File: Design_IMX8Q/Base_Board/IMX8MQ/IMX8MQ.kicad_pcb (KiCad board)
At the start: 8 copper layers, 50.2 x 82 mm, 102 parts, among them Q1 AO3401A, U1 MIMX8MQ6CVAHZAB, U10 PCMF3USB3S, U11 PCMF3USB3S, U12 PCMF3USB3S, U13 KSZ9131RNXI, U14 IMX6ModuleConector_300, U2 IS43LQ32256A-062BLI, U4 MP8759GD-Z, U5 MP2263GD-Z, U6 SDINBDG4-8G, U7 MT25QUxxxxxx1xW7, U9 PTN36043ABXY, X1 ABLNO, Y1 27MHz, Y2 25MHz

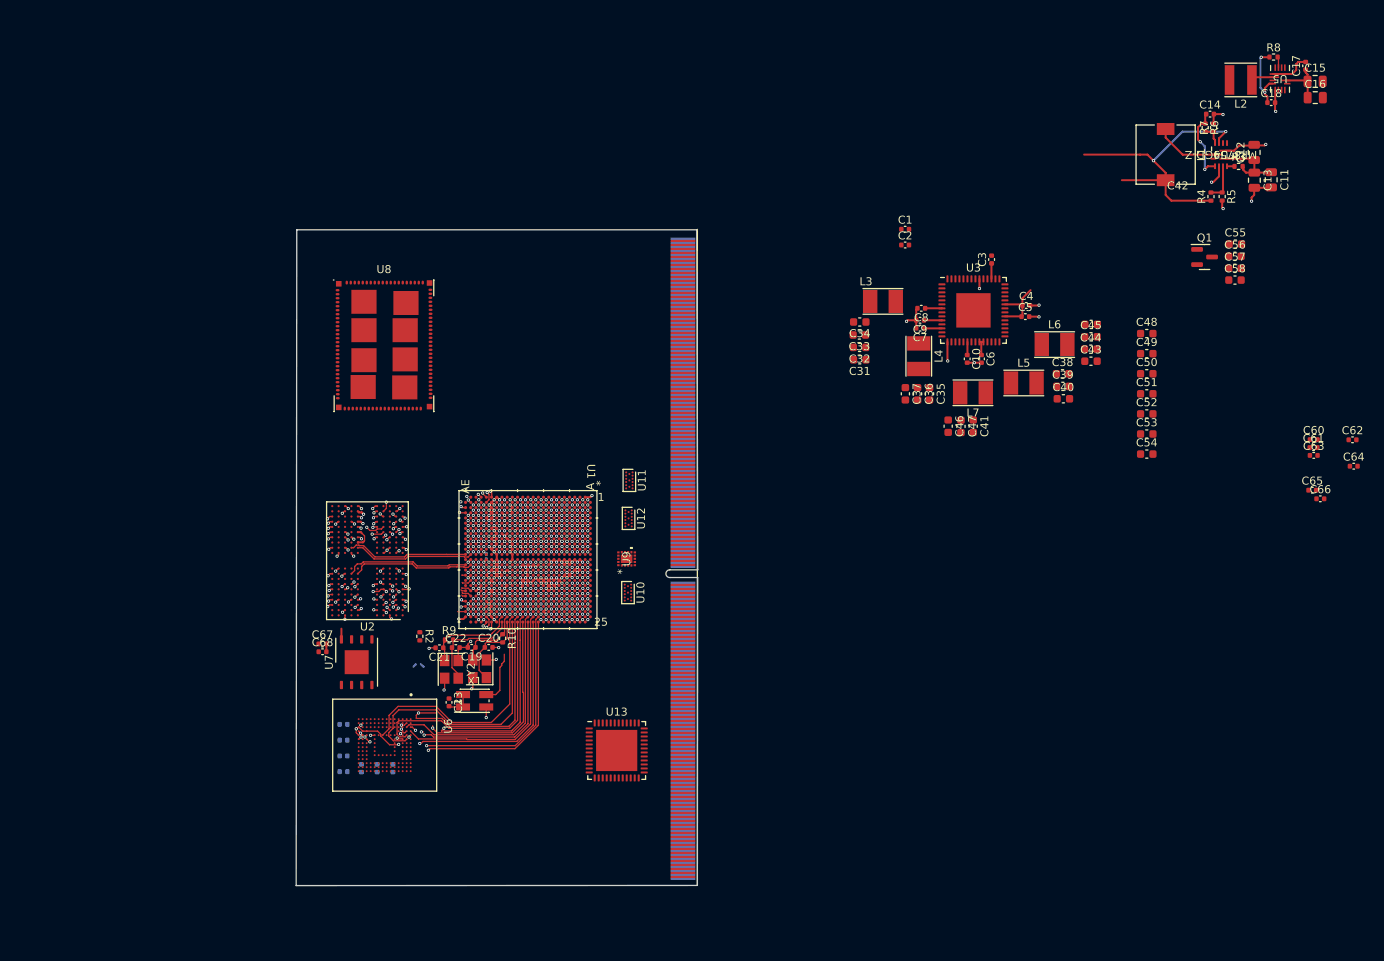
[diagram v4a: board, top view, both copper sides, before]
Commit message: Add QSPI and more color
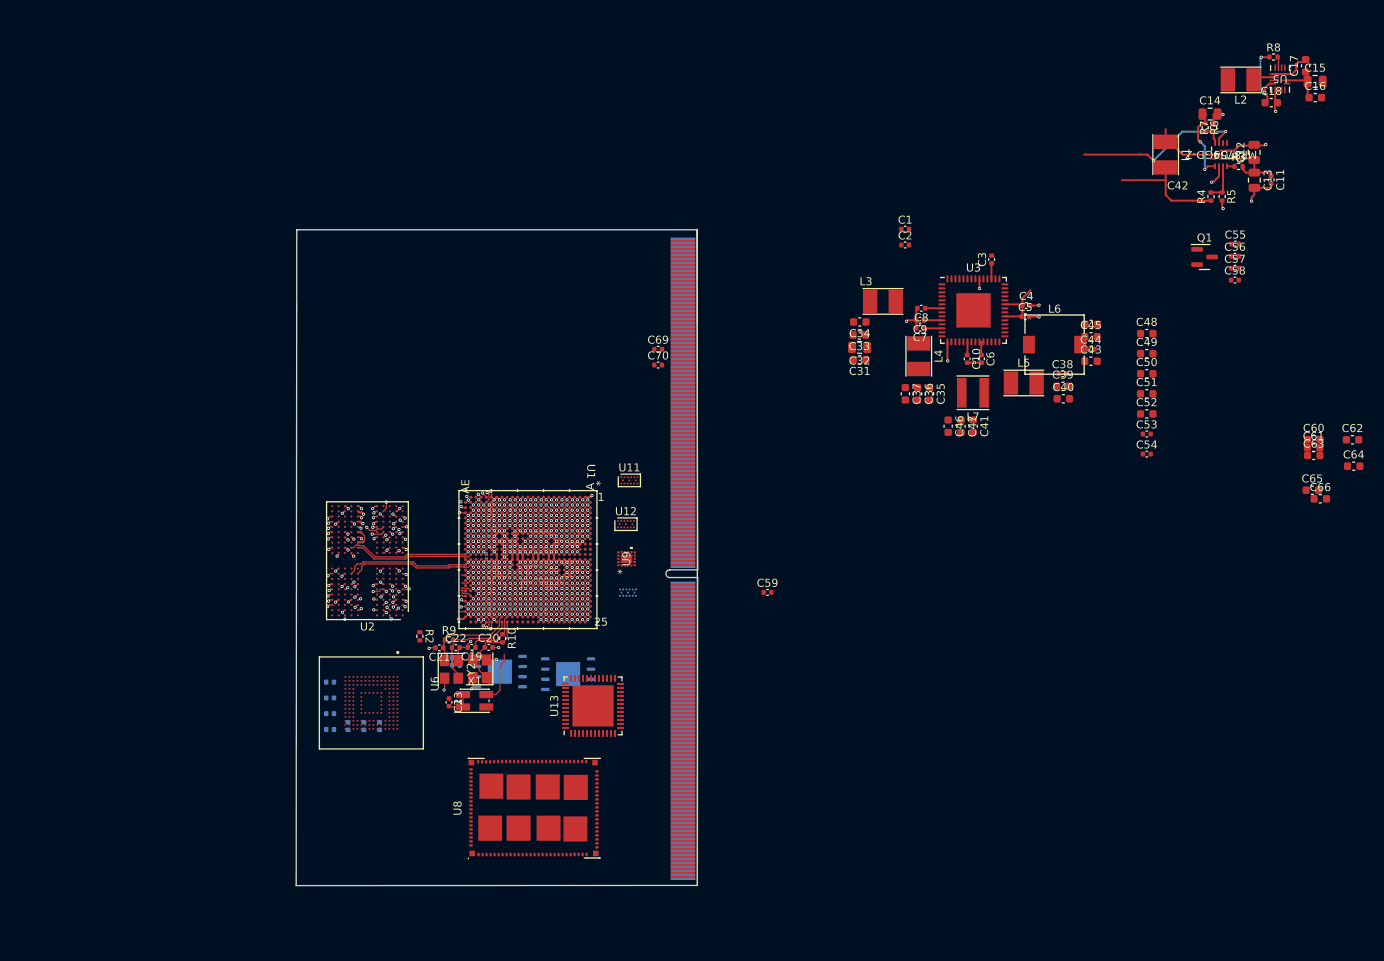
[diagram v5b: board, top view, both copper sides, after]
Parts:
- added C59: 0.1uF, Capacitor_SMD:C_0402_1005Metric, F.Cu at (116.7, 87.0)
- added C69: 0.1uF, Capacitor_SMD:C_0402_1005Metric, F.Cu at (103.0, 56.6)
- added C70: 0.1uF, Capacitor_SMD:C_0402_1005Metric, F.Cu at (103.0, 58.6)
- added U15: MT25QUxxxxxx1xW7, Package_DFN_QFN:W-PDFN-8-1EP_6x5mm_P1.27mm_EP3x3mm, B.Cu at (91.8, 97.2)
- C11: footprint Capacitor_SMD:C_0805_2012Metric -> Capacitor_SMD:C_0402_1005Metric
- C14: footprint Capacitor_SMD:C_0402_1005Metric -> Capacitor_SMD:C_0805_2012Metric
- C16: value 10uF -> 22uF; footprint Capacitor_SMD:C_0805_2012Metric -> Capacitor_SMD:C_0603_1608Metric
- C17: value 0.1uF -> 22uF; footprint Capacitor_SMD:C_0402_1005Metric -> Capacitor_SMD:C_0603_1608Metric
- C18: value 1uF -> 22uF; footprint Capacitor_SMD:C_0402_1005Metric -> Capacitor_SMD:C_0603_1608Metric
- C32: value 22uF -> 10uF; footprint Capacitor_SMD:C_0603_1608Metric -> Capacitor_SMD:C_0805_2012Metric
- C38, C58: value 22uF -> 0.1uF; footprint Capacitor_SMD:C_0603_1608Metric -> Capacitor_SMD:C_0402_1005Metric
- C44: value 22uF -> 1uF; footprint Capacitor_SMD:C_0603_1608Metric -> Capacitor_SMD:C_0402_1005Metric
- C49, C50, C51, C52: value 4.7uF -> 22uF
- C53: value 4.7uF -> 1uF; footprint Capacitor_SMD:C_0603_1608Metric -> Capacitor_SMD:C_0402_1005Metric
- C54: value 1uF -> 0.1uF; footprint Capacitor_SMD:C_0603_1608Metric -> Capacitor_SMD:C_0402_1005Metric
- C55, C56, C57: value 22uF -> 0.47uF; footprint Capacitor_SMD:C_0603_1608Metric -> Capacitor_SMD:C_0402_1005Metric
- C60, C61, C62: value 0.47uF -> 4.7uF; footprint Capacitor_SMD:C_0402_1005Metric -> Capacitor_SMD:C_0603_1608Metric
- C63: value 1uF -> 4.7uF; footprint Capacitor_SMD:C_0402_1005Metric -> Capacitor_SMD:C_0603_1608Metric
- C64, C65: value 0.1uF -> 4.7uF; footprint Capacitor_SMD:C_0402_1005Metric -> Capacitor_SMD:C_0603_1608Metric
- C66: value 0.1uF -> 1uF; footprint Capacitor_SMD:C_0402_1005Metric -> Capacitor_SMD:C_0603_1608Metric
- C67, C68, U10, U7: moved to B.Cu
- L1: value 1.5uH -> 1uH; footprint Inductor_SMD:L_7.3x7.3_H4.5 -> Inductor_SMD:L_Taiyo-Yuden_NR-30xx_HandSoldering
- L2: value 4.7uH -> 1uH; footprint Inductor_SMD:L_Taiyo-Yuden_NR-40xx -> Inductor_SMD:L_Taiyo-Yuden_NR-30xx_HandSoldering
- L6: value 1uH -> 1.5uH; footprint Inductor_SMD:L_Taiyo-Yuden_NR-30xx_HandSoldering -> Inductor_SMD:L_7.3x7.3_H4.5
- L7: value 1uH -> 4.7uH; footprint Inductor_SMD:L_Taiyo-Yuden_NR-30xx_HandSoldering -> Inductor_SMD:L_Taiyo-Yuden_NR-40xx
- R3: value 1.5M -> 100k
- R4: value 44.2K -> 100k
- R5: value 9.53k -> 1.5M
- R6: value 100k -> 44.2K
- R7: value 100k -> 9.53k
- moved U8 60.8 mm to (87.5, 114.0), turned to 90 degrees
- moved U7 17.9 mm to (83.2, 96.9), turned to 0 degrees
- moved C67 16.8 mm to (77.7, 95.1), turned to 180 degrees
- moved C68 16.8 mm to (77.7, 96.1), turned to 180 degrees
- moved U13 6.31 mm to (94.9, 101.2), turned to 90 degrees
- moved C24 5.54 mm to (62.0, 104.1)
- moved C25 5.54 mm to (62.0, 102.2)
- moved C26 5.54 mm to (62.0, 100.2)
- moved C27 5.54 mm to (62.0, 98.2)
- moved C28 5.54 mm to (64.2, 103.7)
- moved C29 5.54 mm to (66.2, 103.7)
- moved C30 5.54 mm to (68.2, 103.7)
- moved U6 5.54 mm to (67.2, 100.8)
- moved U12 0.79 mm to (99.0, 78.5), turned to 0 degrees
- turned U10 to 0 degrees
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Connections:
- C11 pad 1: VSYS -> Net-(U4-VCC)
- C14 pad 1: Net-(U4-VCC) -> VSYS
- C16 pad 1: VSYS -> VDD_GPU_0V9
- C17 pad 1: VSYS -> VDD_VPU_0V9
- C18 pad 1: Net-(U5-VCC) -> NVCC_DRAM_1V1
- C28 pad 2: VDD_3V3 -> NVCC_3V3
- C29 pad 2: VDD_3V3 -> NVCC_3V3
- C30 pad 2: VDD_3V3 -> NVCC_3V3
- C31 pad 1: VDD_GPU_0V9 -> NVCC_SD1_1V8
- C32 pad 1: VDD_GPU_0V9 -> VSYS
- C33 pad 1: VDD_GPU_0V9 -> Net-(U3A-SW3AFB)
- C36 pad 1: VDD_VPU_0V9 -> NVCC_DRAM_1V1
- C37 pad 1: VDD_VPU_0V9 -> NVCC_SD1_1V8
- C38 pad 1: NVCC_DRAM_1V1 -> VSYS
- C39 pad 1: NVCC_DRAM_1V1 -> Net-(U3A-SW3AFB)
- C40 pad 1: NVCC_DRAM_1V1 -> VDD_GPU_0V9
- C41 pad 1: NVCC_SD1_1V8 -> VDD_VPU_0V9
- C42 pad 1: Net-(U3A-SW3AFB) -> NVCC_DRAM_1V1
- C43 pad 1: Net-(U3A-SW3AFB) -> NVCC_SD1_1V8
- C44 pad 1: Net-(U3A-SW3AFB) -> Net-(U5-VCC)
- C46 pad 1: NVCC_SD1_1V8 -> VDD_GPU_0V9
- C47 pad 1: NVCC_SD1_1V8 -> Net-(U3A-SW3AFB)
- C49 pad 1: Net-(U3C-VGEN2) -> DCDC_3V3
- C50 pad 1: Net-(U3C-VGEN3) -> DCDC_3V3
- C51 pad 1: Net-(U3C-VGEN4) -> DCDC_3V3
- C52 pad 1: Net-(U3C-VGEN6) -> DCDC_3V3
- C53 pad 1: Net-(U3C-VSNVS) -> DCDC_3V3
- C54 pad 1: Net-(U3C-VREFDDR) -> Net-(U3C-LICELL)
- C57 pad 1: DCDC_3V3 -> Net-(U3C-VIN3)
- C58 pad 1: DCDC_3V3 -> NVCC_DRAM_1V1
- C58 pad 2: GND -> Net-(U3C-VHALF)
- C60 pad 1: DCDC_3V3 -> Net-(U3C-VGEN1)
- C61 pad 1: DCDC_3V3 -> Net-(U3C-VGEN2)
- C62 pad 1: Net-(U3C-VIN3) -> Net-(U3C-VGEN3)
- C63 pad 1: DCDC_3V3 -> Net-(U3C-VGEN4)
- C64 pad 1: Net-(U3C-LICELL) -> Net-(U3C-VGEN6)
- C65 pad 1: NVCC_DRAM_1V1 -> Net-(U3C-VSNVS)
- C65 pad 2: Net-(U3C-VHALF) -> GND
- C66 pad 1: Net-(U3C-VHALF) -> Net-(U3C-VREFDDR)
- C67 pad 2: VDD_3V3 -> NVCC_3V3
- C68 pad 2: VDD_3V3 -> NVCC_3V3
- L1 pad 1: Net-(U4-SW) -> Net-(U3A-SW1ALX)
- L1 pad 2: DCDC_3V3 -> VDD_GPU_0V9
- L2 pad 1: Net-(U5-SW) -> Net-(U3A-SW1CLX)
- L2 pad 2: DCDC_5V -> VDD_VPU_0V9
- L3 pad 1: Net-(U3A-SW1ALX) -> Net-(U3A-SW2LX)
- L3 pad 2: VDD_GPU_0V9 -> NVCC_DRAM_1V1
- L4 pad 1: Net-(U3A-SW1CLX) -> Net-(U3A-SW4LX)
- L4 pad 2: VDD_VPU_0V9 -> NVCC_SD1_1V8
- L5 pad 1: Net-(U3A-SW2LX) -> Net-(U3A-SW3ALX)
- L5 pad 2: NVCC_DRAM_1V1 -> Net-(U3A-SW3AFB)
- L6 pad 1: Net-(U3A-SW3ALX) -> Net-(U4-SW)
- L6 pad 2: Net-(U3A-SW3AFB) -> DCDC_3V3
- L7 pad 1: Net-(U3A-SW4LX) -> Net-(U5-SW)
- L7 pad 2: NVCC_SD1_1V8 -> DCDC_5V
- Q1 pad 2: VDD_3V3 -> NVCC_3V3
- R3 pad 1: Net-(U4-EN) -> Net-(U4-VCC)
- R3 pad 2: VSYS -> Net-(U4-MODE)
- R4 pad 1: DCDC_3V3 -> Net-(U4-MODE)
- R4 pad 2: Net-(U4-FB) -> GND
- R5 pad 1: Net-(U4-FB) -> Net-(U4-EN)
- R5 pad 2: GND -> VSYS
- R6 pad 1: Net-(U4-VCC) -> DCDC_3V3
- R6 pad 2: Net-(U4-MODE) -> Net-(U4-FB)
- R7 pad 1: Net-(U4-MODE) -> Net-(U4-FB)
- U1 pad A5: unconnected-(U1B-ECSPI2_SS0-PadA5) -> ECSPI2_SS0
- U1 pad A7: unconnected-(U1E-UART1_TXD-PadA7) -> UART1_TXD
- U1 pad AB3: Net-(U1G-NVCC_DRAM-PadAA10) -> NVCC_DRAM_1V1
- U1 pad AB8: Net-(U1G-NVCC_DRAM-PadAA10) -> NVCC_DRAM_1V1
- U1 pad AC3: Net-(U1G-NVCC_DRAM-PadAA10) -> NVCC_DRAM_1V1
- U1 pad AC6: Net-(U1G-NVCC_DRAM-PadAA10) -> NVCC_DRAM_1V1
- U1 pad AC8: Net-(U1G-NVCC_DRAM-PadAA10) -> NVCC_DRAM_1V1
- U1 pad AD5: Net-(U1G-NVCC_DRAM-PadAA10) -> NVCC_DRAM_1V1
- U1 pad B11: unconnected-(U1F-USB2_RESREF-PadB11) -> USB2_VBUS
- U1 pad B2: unconnected-(U1E-SAI1_TXD2-PadB2) -> SAI1_TXD2
- U1 pad B3: unconnected-(U1E-SAI1_TXD6-PadB3) -> SAI1_TXD6
- U1 pad B5: unconnected-(U1B-ECSPI2_MISO-PadB5) -> ECSPI2_MISO
- U1 pad B6: unconnected-(U1E-UART2_RXD-PadB6) -> UART2_RXD
- U1 pad C1: unconnected-(U1E-SAI1_TXD7-PadC1) -> SAI1_TXD7
- U1 pad C11: unconnected-(U1H-USB2_VPTX-PadC11) -> Net-(U1H-USB1_DVDD)
- U1 pad C12: unconnected-(U1H-USB1_VPTX-PadC12) -> Net-(U1H-USB1_DVDD)
- U1 pad C18: unconnected-(U1G-MIPI_VDDHA-PadC18) -> VDD_PHY_1V8
- U1 pad C2: unconnected-(U1E-SAI1_TXD5-PadC2) -> SAI1_TXD5
- U1 pad C3: unconnected-(U1E-SAI3_TXD-PadC3) -> SAI3_TXD
- U1 pad C4: unconnected-(U1E-SAI3_TXC-PadC4) -> SAI3_TXC
- U1 pad C5: unconnected-(U1B-ECSPI2_SCLK-PadC5) -> ECSPI2_SCLK
- U1 pad C6: unconnected-(U1E-UART4_RXD-PadC6) -> UART2_CTS_B
- U1 pad C7: unconnected-(U1E-UART1_RXD-PadC7) -> UART1_RXD
- U1 pad C9: unconnected-(U1F-USB2_ID-PadC9) -> USB2_ID
- U1 pad D1: unconnected-(U1E-SAI1_TXD3-PadD1) -> SAI1_TXD3
- U1 pad D11: unconnected-(U1H-USB2_VP-PadD11) -> Net-(U1H-USB1_DVDD)
- U1 pad D12: unconnected-(U1H-USB1_VP-PadD12) -> Net-(U1H-USB1_DVDD)
- U1 pad D17: unconnected-(U1G-MIPI_VDDHA-PadD17) -> VDD_PHY_1V8
- U1 pad D18: unconnected-(U1G-MIPI_VDDHA-PadD18) -> VDD_PHY_1V8
- U1 pad D2: unconnected-(U1E-SAI1_TXD4-PadD2) -> SAI1_TXD4
- U1 pad D3: unconnected-(U1E-SAI3_MCLK-PadD3) -> SAI3_MCLK
- U1 pad D6: unconnected-(U1E-UART2_TXD-PadD6) -> UART2_TXD
- U1 pad D7: unconnected-(U1E-UART4_TXD-PadD7) -> UART2_RTS_B
- U1 pad D8: unconnected-(U1H-NVCC_UART-PadD8) -> NVCC_3V3
- U1 pad D9: unconnected-(U1F-USB2_VBUS-PadD9) -> USB2_VBUS
- U1 pad E11: unconnected-(U1H-USB2_DVDD-PadE11) -> Net-(U1H-USB1_DVDD)
- U1 pad E12: unconnected-(U1H-USB1_DVDD-PadE12) -> Net-(U1H-USB1_DVDD)
- U1 pad E15: unconnected-(U1G-MIPI_VDD-PadE15) -> VDD_PHY_1V8
- U1 pad E17: unconnected-(U1G-MIPI_VDDA-PadE17) -> VDD_PHY_1V8
- U1 pad E18: unconnected-(U1G-MIPI_VDDA-PadE18) -> VDD_PHY_1V8
- U1 pad E2: unconnected-(U1E-SAI1_TXD1-PadE2) -> SAI1_TXD1
- U1 pad E3: unconnected-(U1H-NVCC_SAI3-PadE3) -> NVCC_3V3
- U1 pad E5: unconnected-(U1B-ECSPI2_MOSI-PadE5) -> ECSPI2_MOSI
- U1 pad E7: unconnected-(U1C-I2C1_SCL-PadE7) -> I2C1_SCL
- U1 pad E8: unconnected-(U1C-I2C1_SDA-PadE8) -> I2C1_SDA
- U1 pad E9: unconnected-(U1C-I2C3_SDA-PadE9) -> I2C3_SDA
- U1 pad F1: unconnected-(U1E-SAI1_RXD5-PadF1) -> SAI1_RXD5
- U1 pad F11: unconnected-(U1H-USB2_VPH-PadF11) -> NVCC_3V3
- U1 pad F12: unconnected-(U1H-USB1_VPH-PadF12) -> NVCC_3V3
- U1 pad F15: unconnected-(U1G-MIPI_VDD-PadF15) -> VDD_PHY_1V8
- U1 pad F17: unconnected-(U1G-MIPI_VDDA-PadF17) -> VDD_PHY_1V8
- U1 pad F18: unconnected-(U1G-MIPI_VDDA-PadF18) -> VDD_PHY_1V8
- U1 pad F19: unconnected-(U1G-MIPI_VDDPLL-PadF19) -> VDD_PHY_1V8
- U1 pad F2: unconnected-(U1E-SAI1_TXD0-PadF2) -> SAI1_TXD0
- U1 pad F21: unconnected-(U1D-NAND_CE2_B-PadF21) -> NAND_CE2_B
- U1 pad F22: unconnected-(U1H-PCIE_VP-PadF22) -> VDD_PHY_0V9
- U1 pad F23: unconnected-(U1H-PCIE_VPTXC-PadF23) -> VDD_PHY_0V9
- U1 pad F3: unconnected-(U1E-SAI3_RXD-PadF3) -> SAI3_RXD
- U1 pad F4: unconnected-(U1E-SAI3_RXC-PadF4) -> SAI3_RXC
- U1 pad F5: unconnected-(U1H-NVCC_ECSPI-PadF5) -> NVCC_3V3
- U1 pad F7: unconnected-(U1C-I2C2_SDA-PadF7) -> I2C2_SDA
- U1 pad F8: unconnected-(U1C-I2C4_SCL-PadF8) -> I2C4_SCL
- U1 pad F9: unconnected-(U1C-I2C4_SDA-PadF9) -> I2C4_SDA
- U1 pad G1: unconnected-(U1E-SAI1_RXD7-PadG1) -> SAI1_RXD7
- U1 pad G11: unconnected-(U1H-USB2_VDD33-PadG11) -> NVCC_3V3
- U1 pad G12: unconnected-(U1H-USB1_VDD33-PadG12) -> NVCC_3V3
- U1 pad G14: unconnected-(U1H-VDD_ARM-PadG14) -> VDD_ARM_0V9
- U1 pad G15: unconnected-(U1H-VDD_ARM-PadG15) -> VDD_ARM_0V9
- U1 pad G16: unconnected-(U1H-VDD_ARM-PadG16) -> VDD_ARM_0V9
- U1 pad G19: unconnected-(U1D-NAND_ALE-PadG19) -> NAND_ALE
- U1 pad G2: unconnected-(U1E-SAI1_RXD6-PadG2) -> SAI1_RXD6
- U1 pad G21: unconnected-(U1D-NAND_CE1_B-PadG21) -> NAND_CE1_B
- U1 pad G22: unconnected-(U1H-PCIE_VP-PadG22) -> VDD_PHY_0V9
- U1 pad G23: unconnected-(U1H-PCIE_VPTXC-PadG23) -> VDD_PHY_0V9
- U1 pad G3: unconnected-(U1E-SAI3_TXFS-PadG3) -> SAI3_TXFS
- U1 pad G4: unconnected-(U1E-SAI3_RXFS-PadG4) -> SAI3_RXFS
- U1 pad G7: unconnected-(U1C-I2C2_SCL-PadG7) -> I2C2_SCL
- U1 pad G8: unconnected-(U1C-I2C3_SCL-PadG8) -> I2C3_SCL
- U1 pad H14: unconnected-(U1H-VDD_ARM-PadH14) -> VDD_ARM_0V9
- U1 pad H15: unconnected-(U1H-VDD_ARM-PadH15) -> VDD_ARM_0V9
- U1 pad H16: unconnected-(U1H-VDD_ARM-PadH16) -> VDD_ARM_0V9
- U1 pad H19: unconnected-(U1D-NAND_CE0_B-PadH19) -> NAND_CE0_B
- U1 pad H2: unconnected-(U1E-SAI1_RXD2-PadH2) -> SAI1_RXD2
- U1 pad H20: unconnected-(U1D-NAND_CE3_B-PadH20) -> NAND_CE3_B
- U1 pad H21: unconnected-(U1D-NAND_CLE-PadH21) -> NAND_CLE
- U1 pad H23: unconnected-(U1H-PCIE_VPH-PadH23) -> NVCC_3V3
- U1 pad H7: unconnected-(U1H-NVCC_I2C-PadH7) -> NVCC_3V3
- U1 pad J1: unconnected-(U1E-SAI1_RXD4-PadJ1) -> SAI1_RXD4
- U1 pad J10: unconnected-(U1H-VDD_GPU-PadJ10) -> VDD_GPU_0V9
- U1 pad J15: unconnected-(U1H-VDD_ARM-PadJ15) -> VDD_ARM_0V9
- U1 pad J16: unconnected-(U1H-VDD_ARM-PadJ16) -> VDD_ARM_0V9
- U1 pad J2: unconnected-(U1E-SAI1_RXD3-PadJ2) -> SAI1_RXD3
- U1 pad J23: unconnected-(U1H-PCIE_VPH-PadJ23) -> NVCC_3V3
- U1 pad J7: unconnected-(U1H-NVCC_SAI2-PadJ7) -> NVCC_3V3
- U1 pad J9: unconnected-(U1H-VDD_GPU-PadJ9) -> VDD_GPU_0V9
- U1 pad K10: VDD_GPU -> VDD_GPU_0V9
- U1 pad K12: VDD_SOC -> VDD_SOC_0v9
- U1 pad K15: VDD_ARM -> VDD_ARM_0V9
- U1 pad K16: VDD_ARM -> VDD_ARM_0V9
- U1 pad K19: unconnected-(U1D-NAND_RE_B-PadK19) -> NAND_RE_B
- U1 pad K2: unconnected-(U1E-SAI1_RXD0-PadK2) -> SAI1_RXD0
- U1 pad K20: unconnected-(U1D-NAND_READY_B-PadK20) -> NAND_READY_B
- U1 pad K21: unconnected-(U1D-NAND_WP_B-PadK21) -> NAND_WP_B
- U1 pad K22: unconnected-(U1D-NAND_WE_B-PadK22) -> NAND_WE_B
- U1 pad K3: unconnected-(U1G-NVCC_SAI1-PadK3) -> NVCC_3V3
- U1 pad K6: unconnected-(U1C-GPIO1_IO13-PadK6) -> USB1_OTG_OC
- U1 pad K9: unconnected-(U1H-VDD_GPU-PadK9) -> VDD_GPU_0V9
- U1 pad L10: VDD_GPU -> VDD_GPU_0V9
- U1 pad L12: VDD_SOC -> VDD_SOC_0v9
- U1 pad L13: VDD_SOC -> VDD_SOC_0v9
- U1 pad L15: VDD_ARM -> VDD_ARM_0V9
- U1 pad L16: VDD_ARM -> VDD_ARM_0V9
- U1 pad L18: Net-(U1G-NVCC_DRAM-PadAA10) -> NVCC_3V3
- U1 pad L2: unconnected-(U1E-SAI1_RXD1-PadL2) -> SAI1_RXD1
- U1 pad L23: unconnected-(U1D-NVCC_SD1-PadL23) -> NVCC_SD1_1V8
- U1 pad L3: unconnected-(U1G-NVCC_SAI1-PadL3) -> NVCC_3V3
- U1 pad L7: unconnected-(U1C-GPIO1_IO12-PadL7) -> USB1_OTG_PWR
- U1 pad L9: unconnected-(U1H-VDD_GPU-PadL9) -> VDD_GPU_0V9
- U1 pad M10: VDD_GPU -> VDD_GPU_0V9
- U1 pad M12: VDD_SOC -> VDD_SOC_0v9
- U1 pad M13: VDD_SOC -> VDD_SOC_0v9
- U1 pad M15: VDD_ARM -> VDD_ARM_0V9
- U1 pad M16: VDD_ARM -> VDD_ARM_0V9
- U1 pad M18: Net-(U1G-NVCC_DRAM-PadAA10) -> NVCC_3V3
- U1 pad M20: unconnected-(U1D-NAND_DQS-PadM20) -> NAND_DQS
- U1 pad M23: unconnected-(U1D-NVCC_SD1-PadM23) -> NVCC_SD1_1V8
- U1 pad M3: unconnected-(U1H-NVCC_SAI5-PadM3) -> NVCC_3V3
- U1 pad M7: unconnected-(U1C-GPIO1_IO10-PadM7) -> USB1_OTG_ID
- U1 pad M9: unconnected-(U1H-VDD_GPU-PadM9) -> VDD_GPU_0V9
- U1 pad N10: VDD_VPU -> VDD_VPU_0V9
- U1 pad N13: VDD_SOC -> VDD_SOC_0v9
- U1 pad N23: unconnected-(U1D-NVCC_SD2-PadN23) -> NVCC_SD2
- U1 pad N8: unconnected-(U1H-VDD_VPU-PadN8) -> VDD_VPU_0V9
- U1 pad N9: unconnected-(U1H-VDD_VPU-PadN9) -> VDD_VPU_0V9
- U1 pad P10: VDD_VPU -> VDD_VPU_0V9
- U1 pad P12: VDD_SOC -> VDD_SOC_0v9
- U1 pad P13: VDD_SOC -> VDD_SOC_0v9
- U1 pad P15: VDD_SOC -> VDD_SOC_0v9
- U1 pad P16: VDD_SOC -> VDD_SOC_0v9
- U1 pad P2: unconnected-(U1G-HDMI_AVDDIO-PadP2) -> VDD_PHY_1V8
- U1 pad P9: unconnected-(U1H-VDD_VPU-PadP9) -> VDD_VPU_0V9
- U1 pad R10: VDD_SOC -> VDD_SOC_0v9
- U1 pad R11: VDD_SOC -> VDD_SOC_0v9
- U1 pad R12: VDD_SOC -> VDD_SOC_0v9
- U1 pad R13: VDD_SOC -> VDD_SOC_0v9
- U1 pad R14: VDD_SOC -> VDD_SOC_0v9
- U1 pad R15: VDD_SOC -> VDD_SOC_0v9
- U1 pad R16: VDD_SOC -> VDD_SOC_0v9
- U1 pad R5: unconnected-(U1G-NVCC_GPIO1-PadR5) -> NVCC_3V3
- U1 pad R6: unconnected-(U1G-NVCC_GPIO1-PadR6) -> NVCC_3V3
- U1 pad R8: unconnected-(U1H-VDD_SOC-PadR8) -> VDD_SOC_0v9
- U1 pad R9: unconnected-(U1H-VDD_SOC-PadR9) -> VDD_SOC_0v9
- U1 pad T17: VDD_SOC -> VDD_SOC_0v9
- U1 pad T18: unconnected-(U1H-NVCC_ENET-PadT18) -> NVCC_ENET_2V5
- U1 pad T8: unconnected-(U1H-VDD_SOC-PadT8) -> VDD_SOC_0v9
- U1 pad U10: Net-(U1H-VDD_DRAM-PadU10) -> VDD_DRAM_0V9
- U1 pad U11: Net-(U1H-VDD_DRAM-PadU10) -> VDD_DRAM_0V9
- U1 pad U12: Net-(U1H-VDD_DRAM-PadU10) -> VDD_DRAM_0V9
- U1 pad U13: Net-(U1H-VDD_DRAM-PadU10) -> VDD_DRAM_0V9
- U1 pad U14: Net-(U1H-VDD_DRAM-PadU10) -> VDD_DRAM_0V9
- U1 pad U3: unconnected-(U1G-HDMI_AVDDCORE-PadU3) -> VDD_PHY_0V9
- U1 pad U4: unconnected-(U1G-HDMI_AVDDCORE-PadU4) -> VDD_PHY_0V9
- U1 pad V10: Net-(U1H-VDD_DRAM-PadU10) -> VDD_DRAM_0V9
- U1 pad V11: Net-(U1H-VDD_DRAM-PadU10) -> VDD_DRAM_0V9
- U1 pad V12: Net-(U1H-VDD_DRAM-PadU10) -> VDD_DRAM_0V9
- U1 pad V13: Net-(U1H-VDD_DRAM-PadU10) -> VDD_DRAM_0V9
- U1 pad V14: Net-(U1H-VDD_DRAM-PadU10) -> VDD_DRAM_0V9
- U1 pad V15: Net-(U1H-VDD_DRAM-PadU10) -> VDD_DRAM_0V9
- U1 pad V3: unconnected-(U1G-HDMI_AVDDCLK-PadV3) -> VDD_PHY_0V9
- U1 pad V9: unconnected-(U1H-VDD_DRAM-PadV9) -> VDD_DRAM_0V9
- U1 pad W18: unconnected-(U1H-NVCC_SNVS-PadW18) -> NVCC_3V3
- U1 pad W4: unconnected-(U1H-NVCC_JTAG-PadW4) -> NVCC_3V3
- U1 pad Y10: Net-(U1H-VDD_DRAM-PadU10) -> VDD_DRAM_0V9
- U1 pad Y16: Net-(U1H-VDD_DRAM-PadU10) -> VDD_DRAM_0V9
- U1 pad Y18: Net-(U1H-VDD_DRAM-PadU10) -> VDD_DRAM_0V9
- U1 pad Y20: Net-(U1H-VDD_DRAM-PadU10) -> VDD_DRAM_0V9
- U1 pad Y6: unconnected-(U1H-VDD_DRAM-PadY6) -> VDD_DRAM_0V9
- U1 pad Y8: unconnected-(U1H-VDD_DRAM-PadY8) -> VDD_DRAM_0V9
- U14 pad 13: unconnected-(U14-Pad13) -> SAI1_RXD1
- U14 pad 15: unconnected-(U14-Pad15) -> SAI1_RXD0
- U14 pad 17: unconnected-(U14-Pad17) -> SAI1_RXD3
- U14 pad 19: unconnected-(U14-Pad19) -> SAI1_RXD4
- U14 pad 21: unconnected-(U14-Pad21) -> SAI1_RXD2
- U14 pad 23: unconnected-(U14-Pad23) -> SAI1_RXD6
- U14 pad 25: unconnected-(U14-Pad25) -> SAI1_RXD7
- U14 pad 27: unconnected-(U14-Pad27) -> SAI1_TXD0
- U14 pad 29: unconnected-(U14-Pad29) -> SAI1_RXD5
- U14 pad 31: unconnected-(U14-Pad31) -> SAI1_TXD1
- U14 pad 33: unconnected-(U14-Pad33) -> SAI1_TXD4
- U14 pad 35: unconnected-(U14-Pad35) -> SAI1_TXD3
- U14 pad 37: unconnected-(U14-Pad37) -> SAI1_TXD5
- U14 pad 39: unconnected-(U14-Pad39) -> SAI1_TXD7
- U14 pad 41: unconnected-(U14-Pad41) -> SAI1_TXD6
- U14 pad 43: unconnected-(U14-Pad43) -> SAI1_TXD2
- U14 pad 53: unconnected-(U14-Pad53) -> ECSPI2_MOSI
- U14 pad 55: unconnected-(U14-Pad55) -> ECSPI2_SCLK
- U14 pad 57: unconnected-(U14-Pad57) -> ECSPI2_MISO
- U14 pad 59: unconnected-(U14-Pad59) -> ECSPI2_SS0
- U14 pad 62: unconnected-(U14-Pad62) -> UART2_RXD
- U14 pad 63: unconnected-(U14-Pad63) -> I2C1_SCL
- U14 pad 64: unconnected-(U14-Pad64) -> UART2_TXD
- U14 pad 65: unconnected-(U14-Pad65) -> I2C1_SDA
- U14 pad 66: unconnected-(U14-Pad66) -> UART2_CTS_B
- U14 pad 67: unconnected-(U14-Pad67) -> I2C2_SDA
- U14 pad 68: unconnected-(U14-Pad68) -> UART2_RTS_B
- U14 pad 69: unconnected-(U14-Pad69) -> I2C2_SCL
- U14 pad 71: unconnected-(U14-Pad71) -> I2C3_SDA
- U14 pad 73: unconnected-(U14-Pad73) -> I2C3_SCL
- U14 pad 75: unconnected-(U14-Pad75) -> I2C4_SCL
- U14 pad 77: unconnected-(U14-Pad77) -> I2C4_SDA
- U6 pad E6: VDD_3V3 -> NVCC_3V3
- U6 pad F5: VDD_3V3 -> NVCC_3V3
- U6 pad J10: VDD_3V3 -> NVCC_3V3
- U6 pad K9: VDD_3V3 -> NVCC_3V3
- U7 pad 1: unconnected-(U7-~{S}-Pad1) -> NAND_CE0_B
- U7 pad 6: unconnected-(U7-C-Pad6) -> NAND_ALE
- U7 pad 8: VDD_3V3 -> NVCC_3V3
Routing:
- net SD1_DATA7: track 33.3 -> 0.00 mm
- net SD1_STROBE: track 31.2 -> 0.00 mm
- net SD1_DATA6: track 31.1 -> 0.00 mm
- net GND: track 162.7 -> 192.8 mm, vias 599 -> 533
- net SD1_DATA1: track 29.8 -> 0.00 mm
- net SD1_nRST: track 29.6 -> 0.00 mm, vias 2 -> 0
- net SD1_DATA4: track 29.5 -> 0.00 mm, vias 1 -> 0
- net SD1_DATA0: track 28.8 -> 0.00 mm, vias 2 -> 0
- net SD1_CMD: track 28.7 -> 0.00 mm, vias 2 -> 0
- net SD1_CLK: track 28.5 -> 0.00 mm, vias 2 -> 0
- net SD1_DATA2: track 26.9 -> 0.00 mm, vias 3 -> 1
- net SD1_DATA3: track 25.7 -> 0.00 mm, vias 4 -> 2
- net SD1_DATA5: track 25.2 -> 0.00 mm, vias 3 -> 0
- net VDD_SOC_0v9: track 0.00 -> 16.4 mm, vias 0 -> 13
- net VDD_DRAM_0V9: track 0.00 -> 8.27 mm, vias 0 -> 8
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
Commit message: it was inserted power control system
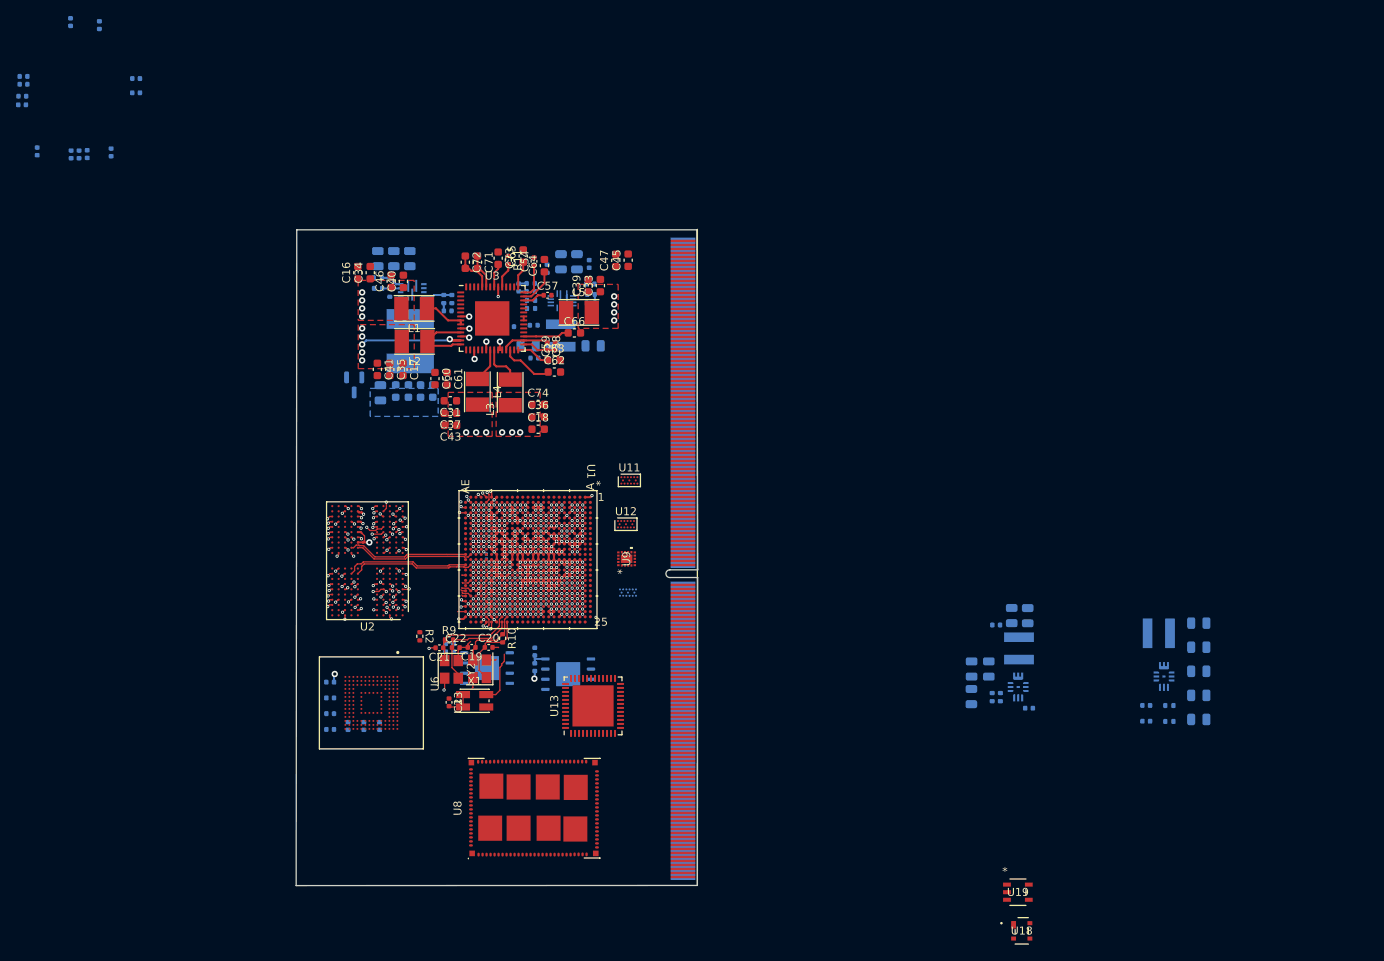
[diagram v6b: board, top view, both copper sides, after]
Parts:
- added C71: 1uF, Capacitor_SMD:C_0603_1608Metric, F.Cu at (80.4, 45.7)
- added C72: 0.22uF, Capacitor_SMD:C_0603_1608Metric, F.Cu at (78.9, 45.7)
- added C73: 1uF, Capacitor_SMD:C_0603_1608Metric, F.Cu at (83.0, 45.2)
- added C74: 22uF, Capacitor_SMD:C_0603_1608Metric, F.Cu at (88.0, 63.5)
- added C75: 10uF, Capacitor_SMD:C_0805_2012Metric, B.Cu at (94.9, 56.2)
- added C76: 0.1uF, Capacitor_SMD:C_0402_1005Metric, B.Cu at (87.5, 57.7)
- added C77: 1uF, Capacitor_SMD:C_0402_1005Metric, B.Cu at (87.4, 53.6)
- added C78: 1uF, Capacitor_SMD:C_0402_1005Metric, B.Cu at (94.2, 52.4)
- added C79: 5.6uF, Capacitor_SMD:C_0402_1005Metric, B.Cu at (85.6, 48.9)
- added C80: 1uF, Capacitor_SMD:C_0402_1005Metric, B.Cu at (84.5, 53.8)
- added C81: 22uF, Capacitor_SMD:C_0805_2012Metric, B.Cu at (142.2, 100.0)
- added C82: 22uF, Capacitor_SMD:C_0805_2012Metric, B.Cu at (144.3, 96.6)
- added C83: 22uF, Capacitor_SMD:C_0805_2012Metric, B.Cu at (142.2, 96.6)
- added C84: 5.6uF, Capacitor_SMD:C_0402_1005Metric, B.Cu at (149.4, 101.5)
- added C85: 10uF, Capacitor_SMD:C_0805_2012Metric, B.Cu at (149.2, 89.9)
- added C86: 10uF, Capacitor_SMD:C_0805_2012Metric, B.Cu at (147.2, 89.9)
- added C87: 0.1uF, Capacitor_SMD:C_0402_1005Metric, B.Cu at (145.3, 91.1)
- added C88: 22uF, Capacitor_SMD:C_0805_2012Metric, B.Cu at (170.6, 90.8)
- added C89: 22uF, Capacitor_SMD:C_0805_2012Metric, B.Cu at (170.6, 93.8)
- added C90: 22uF, Capacitor_SMD:C_0805_2012Metric, B.Cu at (170.6, 96.9)
- added C91: 5.6uF, Capacitor_SMD:C_0402_1005Metric, B.Cu at (164.0, 101.1)
- added C92: 10uF, Capacitor_SMD:C_0805_2012Metric, B.Cu at (170.6, 99.9)
- added C93: 10uF, Capacitor_SMD:C_0805_2012Metric, B.Cu at (170.6, 102.9)
- added C94: 0.1uF, Capacitor_SMD:C_0402_1005Metric, B.Cu at (164.0, 103.1)
- added L8: 4.7uH, Inductor_SMD:L_Taiyo-Yuden_NR-40xx, B.Cu at (148.1, 94.0)
- added L9: 4.7uH, Inductor_SMD:L_Taiyo-Yuden_NR-40xx, B.Cu at (165.6, 92.1)
- added R11: 10.0k, Resistor_SMD:R_0402_1005Metric, F.Cu at (84.3, 45.5)
- added R12: 0K, Resistor_SMD:R_0402_1005Metric, B.Cu at (94.5, 48.5)
- added R13: 27K, Resistor_SMD:R_0402_1005Metric, B.Cu at (89.1, 46.5)
- added R14: 10K, Resistor_SMD:R_0402_1005Metric, B.Cu at (87.1, 48.4)
- added R15: 10K, Resistor_SMD:R_0402_1005Metric, B.Cu at (87.1, 49.4)
- added R16: 0K, Resistor_SMD:R_0402_1005Metric, B.Cu at (87.1, 50.5)
- added R17: 0K, Resistor_SMD:R_0402_1005Metric, B.Cu at (87.1, 51.5)
- added R18: 10K, Resistor_SMD:R_0402_1005Metric, B.Cu at (166.9, 101.1)
- added R19: 10K, Resistor_SMD:R_0402_1005Metric, B.Cu at (145.8, 100.1)
- added R20: 10K, Resistor_SMD:R_0402_1005Metric, B.Cu at (144.8, 100.1)
- added R21: 10K, Resistor_SMD:R_0402_1005Metric, B.Cu at (166.9, 103.1)
- added U16: MP2147GD-P, _W_SBC:MP2147GD-P, B.Cu at (148.0, 98.8)
- added U17: MP2147GD-P, _W_SBC:MP2147GD-P, B.Cu at (166.2, 97.5)
- added U18: UM805RE, _W_SBC:UM805RE, F.Cu at (148.4, 129.3)
- added U19: LDCL015MR, _W_SBC:LDCL015MR, F.Cu at (148.0, 124.5)
- C1, C10, C11, C12, C13, C14, C15, C2, C3, C32, C38, C4, C44, C49, C5, C50, C51, C52, C53, C55, C56, C6, C69, C7, C70, C8, C9, L7, Q1, R3, R4, R5, R6, R7, R8, U4, U5: moved to B.Cu
- C42: value 22uF -> 10uF; footprint Capacitor_SMD:C_0603_1608Metric -> Capacitor_SMD:C_0805_2012Metric; moved to B.Cu
- C48: value 4.7uF -> 220uF; footprint Capacitor_SMD:C_0603_1608Metric -> Capacitor_SMD:C_0805_2012Metric; moved to B.Cu
- L6: footprint Inductor_SMD:L_7.3x7.3_H4.5 -> Inductor_SMD:L_Taiyo-Yuden_NR-60xx_HandSoldering; moved to B.Cu
- moved C55 150.2 mm to (25.4, 31.9), turned to -90 degrees
- moved C53 144.0 mm to (29.6, 15.7), turned to 90 degrees
- moved C56 141.1 mm to (34.6, 32.0), turned to -90 degrees
- moved C3 122.7 mm to (23.5, 26.0), turned to 180 degrees
- moved C16 121.7 mm to (65.5, 47.0), turned to 90 degrees
- moved C4 119.9 mm to (30.6, 32.2), turned to -90 degrees
- moved C17 119.0 mm to (71.1, 59.1), turned to -90 degrees
- moved C5 119.0 mm to (31.6, 32.2), turned to -90 degrees
- moved C7 116.4 mm to (23.7, 22.5)
- moved C9 115.9 mm to (23.7, 23.5)
- moved C8 115.5 mm to (23.5, 25.0)
- moved C6 111.3 mm to (37.7, 22.8), turned to 0 degrees
- moved C60 110.1 mm to (75.1, 60.3), turned to -90 degrees
- moved C13 110.0 mm to (68.0, 45.3), turned to 90 degrees
- moved C10 109.1 mm to (37.7, 24.5), turned to 0 degrees
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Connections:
- net Net-(U3C-VGEN4) renamed VDDA_1V8
- net Net-(U3C-VGEN6) renamed VCAM_2V8
- net Net-(U3C-VREFDDR) renamed VREFDDR
- net Net-(U3C-VSNVS) renamed VDD_SNVS_0V9
- C33 pad 1: Net-(U3A-SW3AFB) -> VDD_DRAM_0V9
- C39 pad 1: Net-(U3A-SW3AFB) -> VDD_DRAM_0V9
- C42 pad 1: NVCC_DRAM_1V1 -> DCDC_5V
- C45 pad 1: Net-(U3A-SW3AFB) -> VDD_DRAM_0V9
- C47 pad 1: Net-(U3A-SW3AFB) -> VDD_DRAM_0V9
- C48 pad 1: Net-(U3C-VGEN1) -> DCDC_3V3
- C60 pad 1: Net-(U3C-VGEN1) -> VCAM_1V5
- C61 pad 1: Net-(U3C-VGEN2) -> VDD_PHY_0V9
- C62 pad 1: Net-(U3C-VGEN3) -> VDD_PHY_1V8
- L5 pad 2: Net-(U3A-SW3AFB) -> VDD_DRAM_0V9
- U1 pad AA10: Net-(U1G-NVCC_DRAM-PadAA10) -> NVCC_DRAM_1V1
- U1 pad AA15: Net-(U1G-NVCC_DRAM-PadAA10) -> NVCC_DRAM_1V1
- U1 pad AB17: Net-(U1G-NVCC_DRAM-PadAA10) -> NVCC_DRAM_1V1
- U1 pad AB23: Net-(U1G-NVCC_DRAM-PadAA10) -> NVCC_DRAM_1V1
- U1 pad AC14: Net-(U1G-NVCC_DRAM-PadAA10) -> NVCC_DRAM_1V1
- U1 pad AC17: Net-(U1G-NVCC_DRAM-PadAA10) -> NVCC_DRAM_1V1
- U1 pad AC20: Net-(U1G-NVCC_DRAM-PadAA10) -> NVCC_DRAM_1V1
- U1 pad AC23: Net-(U1G-NVCC_DRAM-PadAA10) -> NVCC_DRAM_1V1
- U1 pad AD18: Net-(U1G-NVCC_DRAM-PadAA10) -> NVCC_DRAM_1V1
- U1 pad AD21: Net-(U1G-NVCC_DRAM-PadAA10) -> NVCC_DRAM_1V1
- U1 pad H3: unconnected-(U1E-SAI2_RXC-PadH3) -> SAI2_RXC
- U1 pad H4: unconnected-(U1E-SAI2_TXFS-PadH4) -> SAI2_TXFS
- U1 pad H5: unconnected-(U1E-SAI2_MCLK-PadH5) -> SAI2_MCLK
- U1 pad K10: VDD_GPU_0V9 -> unconnected-(U1H-VDD_GPU-PadK10)
- U1 pad K12: VDD_SOC_0v9 -> unconnected-(U1H-VDD_SOC-PadK12)
- U1 pad K15: VDD_ARM_0V9 -> unconnected-(U1H-VDD_ARM-PadK15)
- U1 pad K16: VDD_ARM_0V9 -> unconnected-(U1H-VDD_ARM-PadK16)
- U1 pad L10: VDD_GPU_0V9 -> unconnected-(U1H-VDD_GPU-PadL10)
- U1 pad L12: VDD_SOC_0v9 -> unconnected-(U1H-VDD_SOC-PadL12)
- U1 pad L13: VDD_SOC_0v9 -> unconnected-(U1H-VDD_SOC-PadL13)
- U1 pad L15: VDD_ARM_0V9 -> unconnected-(U1H-VDD_ARM-PadL15)
- U1 pad L16: VDD_ARM_0V9 -> unconnected-(U1H-VDD_ARM-PadL16)
- U1 pad M10: VDD_GPU_0V9 -> unconnected-(U1H-VDD_GPU-PadM10)
- U1 pad M12: VDD_SOC_0v9 -> unconnected-(U1H-VDD_SOC-PadM12)
- U1 pad M13: VDD_SOC_0v9 -> unconnected-(U1H-VDD_SOC-PadM13)
- U1 pad M15: VDD_ARM_0V9 -> unconnected-(U1H-VDD_ARM-PadM15)
- U1 pad M16: VDD_ARM_0V9 -> unconnected-(U1H-VDD_ARM-PadM16)
- U1 pad N10: VDD_VPU_0V9 -> unconnected-(U1H-VDD_VPU-PadN10)
- U1 pad N13: VDD_SOC_0v9 -> unconnected-(U1H-VDD_SOC-PadN13)
- U1 pad P10: VDD_VPU_0V9 -> unconnected-(U1H-VDD_VPU-PadP10)
- U1 pad P12: VDD_SOC_0v9 -> unconnected-(U1H-VDD_SOC-PadP12)
- U1 pad P13: VDD_SOC_0v9 -> unconnected-(U1H-VDD_SOC-PadP13)
- U1 pad P15: VDD_SOC_0v9 -> unconnected-(U1H-VDD_SOC-PadP15)
- U1 pad P16: VDD_SOC_0v9 -> unconnected-(U1H-VDD_SOC-PadP16)
- U1 pad R10: VDD_SOC_0v9 -> unconnected-(U1H-VDD_SOC-PadR10)
- U1 pad R11: VDD_SOC_0v9 -> unconnected-(U1H-VDD_SOC-PadR11)
- U1 pad R12: VDD_SOC_0v9 -> unconnected-(U1H-VDD_SOC-PadR12)
- U1 pad R13: VDD_SOC_0v9 -> unconnected-(U1H-VDD_SOC-PadR13)
- U1 pad R14: VDD_SOC_0v9 -> unconnected-(U1H-VDD_SOC-PadR14)
- U1 pad R15: VDD_SOC_0v9 -> unconnected-(U1H-VDD_SOC-PadR15)
- U1 pad R16: VDD_SOC_0v9 -> unconnected-(U1H-VDD_SOC-PadR16)
- U1 pad T17: VDD_SOC_0v9 -> unconnected-(U1H-VDD_SOC-PadT17)
- U1 pad U10: VDD_DRAM_0V9 -> unconnected-(U1H-VDD_DRAM-PadU10)
- U1 pad U11: VDD_DRAM_0V9 -> unconnected-(U1H-VDD_DRAM-PadU11)
- U1 pad U12: VDD_DRAM_0V9 -> unconnected-(U1H-VDD_DRAM-PadU12)
- U1 pad U13: VDD_DRAM_0V9 -> unconnected-(U1H-VDD_DRAM-PadU13)
- U1 pad U14: VDD_DRAM_0V9 -> unconnected-(U1H-VDD_DRAM-PadU14)
- U1 pad V10: VDD_DRAM_0V9 -> unconnected-(U1H-VDD_DRAM-PadV10)
- U1 pad V11: VDD_DRAM_0V9 -> unconnected-(U1H-VDD_DRAM-PadV11)
- U1 pad V12: VDD_DRAM_0V9 -> unconnected-(U1H-VDD_DRAM-PadV12)
- U1 pad V13: VDD_DRAM_0V9 -> unconnected-(U1H-VDD_DRAM-PadV13)
- U1 pad V14: VDD_DRAM_0V9 -> unconnected-(U1H-VDD_DRAM-PadV14)
- U1 pad V15: VDD_DRAM_0V9 -> unconnected-(U1H-VDD_DRAM-PadV15)
- U1 pad Y10: VDD_DRAM_0V9 -> unconnected-(U1H-VDD_DRAM-PadY10)
- U1 pad Y12: Net-(U1G-NVCC_DRAM-PadAA10) -> NVCC_DRAM_1V1
- U1 pad Y14: Net-(U1G-NVCC_DRAM-PadAA10) -> NVCC_DRAM_1V1
- U1 pad Y16: VDD_DRAM_0V9 -> unconnected-(U1H-VDD_DRAM-PadY16)
- U1 pad Y18: VDD_DRAM_0V9 -> unconnected-(U1H-VDD_DRAM-PadY18)
- U1 pad Y20: VDD_DRAM_0V9 -> unconnected-(U1H-VDD_DRAM-PadY20)
- U14 pad 10: unconnected-(U14-Pad10) -> VSYS
- U14 pad 4: unconnected-(U14-Pad4) -> VSYS
- U14 pad 6: unconnected-(U14-Pad6) -> VSYS
- U14 pad 8: unconnected-(U14-Pad8) -> VSYS
- U3 pad 16: Net-(U3C-VGEN1) -> VCAM_1V5
- U3 pad 18: Net-(U3C-VGEN2) -> VDD_PHY_0V9
- U3 pad 26: Net-(U3C-VGEN3) -> VDD_PHY_1V8
- U3 pad 3: unconnected-(U3B-/RESETBMCU-Pad3) -> POR_B
- U3 pad 38: Net-(U3A-SW3AFB) -> VDD_DRAM_0V9
- U3 pad 39: unconnected-(U3C-VGEN5-Pad39) -> NVCC_3V3
- U3 pad 47: unconnected-(U3B-VDDOTP-Pad47) -> Net-(U3B-VDDOTP)
- U3 pad 49: unconnected-(U3B-VCORE-Pad49) -> Net-(U3B-VCORE)
- U3 pad 51: unconnected-(U3B-VCOREDIG-Pad51) -> Net-(U3B-VCOREDIG)
- U3 pad 52: unconnected-(U3B-VCOREREF-Pad52) -> Net-(U3B-VCOREREF)
- U3 pad 55: unconnected-(U3B-VDDIO-Pad55) -> NVCC_3V3
- U5 pad 10: unconnected-(U5-BST-Pad10) -> Net-(U5-BST)
- U5 pad 13: unconnected-(U5-SS-Pad13) -> Net-(U5-SS)
- U5 pad 14: unconnected-(U5-FB-Pad14) -> Net-(U5-FB)
- U5 pad 15: unconnected-(U5-FREQ-Pad15) -> Net-(U5-FREQ)
- U5 pad 4: unconnected-(U5-EN-Pad4) -> Net-(U5-EN)
- U5 pad 7: unconnected-(U5-BIAS-Pad7) -> Net-(U5-BIAS)
- U8 pad 4: Net-(U8B-VDD-Pad4) -> NVCC_3V3
- U8 pad 72: Net-(U8B-VDD-Pad4) -> NVCC_3V3
- U8 pad 73: Net-(U8B-VDD-Pad4) -> NVCC_3V3
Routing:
- net NVCC_SD1_1V8: track 0.00 -> 61.4 mm, vias 0 -> 6
- net DCDC_3V3: track 58.4 -> 7.04 mm, vias 2 -> 6
- net NVCC_DRAM_1V1: track 2.57 -> 40.7 mm, vias 0 -> 5
- net GND: track 192.8 -> 163.0 mm, vias 533 -> 396
- net VSYS: track 16.9 -> 0.00 mm, vias 1 -> 0
- net VDD_VPU_0V9: track 0.43 -> 16.9 mm, vias 2 -> 9
- net NVCC_3V3: track 1.01 -> 16.1 mm, vias 2 -> 17
- net Net-(U3A-SW1CLX): track 0.00 -> 9.10 mm
- net Net-(U4-VCC): track 9.37 -> 0.97 mm, vias 2 -> 0
- net Net-(U4-SW): track 8.33 -> 0.00 mm
- net Net-(U5-VCC): track 8.87 -> 1.08 mm, vias 2 -> 0
- net VDD_PHY_1V8: track 0.00 -> 6.57 mm
- net VREFDDR: track 0.00 -> 5.74 mm
- net Net-(U3A-SW1ALX): track 0.00 -> 5.34 mm
- net Net-(U3A-SW2LX): track 0.00 -> 5.27 mm
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- added copper zone on In3.Cu, net DCDC_3V3
- added copper zone on B.Cu, net GND
- added copper zone on F.Cu, net NVCC_DRAM_1V1
- added copper zone on F.Cu, net NVCC_SD1_1V8
- added copper zone on F.Cu, net VDD_DRAM_0V9
- added copper zone on F.Cu, net VDD_GPU_0V9
- added copper zone on F.Cu, net VDD_VPU_0V9
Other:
- board text added: "VDD VDD_3V3 -> NVCC_3V3 -> NVCC_JTAG_3V3 -> NVCC_GPUI_3V3 -> NVCC_UART_3V3 -> NVCC_NAND_3V3 -> NVCC_SAI1_3V3 -> NVCC_SAI2_3V3 -> NVCC_SAI3_3V3 -> NVCC_SAI5_3V3 -> NVCC_I2C_3V3 -> NVCC_ECSPI_3V3 NVCC_SD1_1V8 VDD_PHY_3V3 VDD_PHY_1V8 VDD_SOC_0V9 VDD_ARM_0V9 VDD_VPU_0V9 VDD_GPU_0V9 VDD_DRAM_0V9 VDDA_1V8 NVCC_DRAM_1V1"
